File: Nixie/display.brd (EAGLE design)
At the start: 111.4 x 49.5 mm, 21 parts, among them IC1 74LS595N, IC2 74LS595N

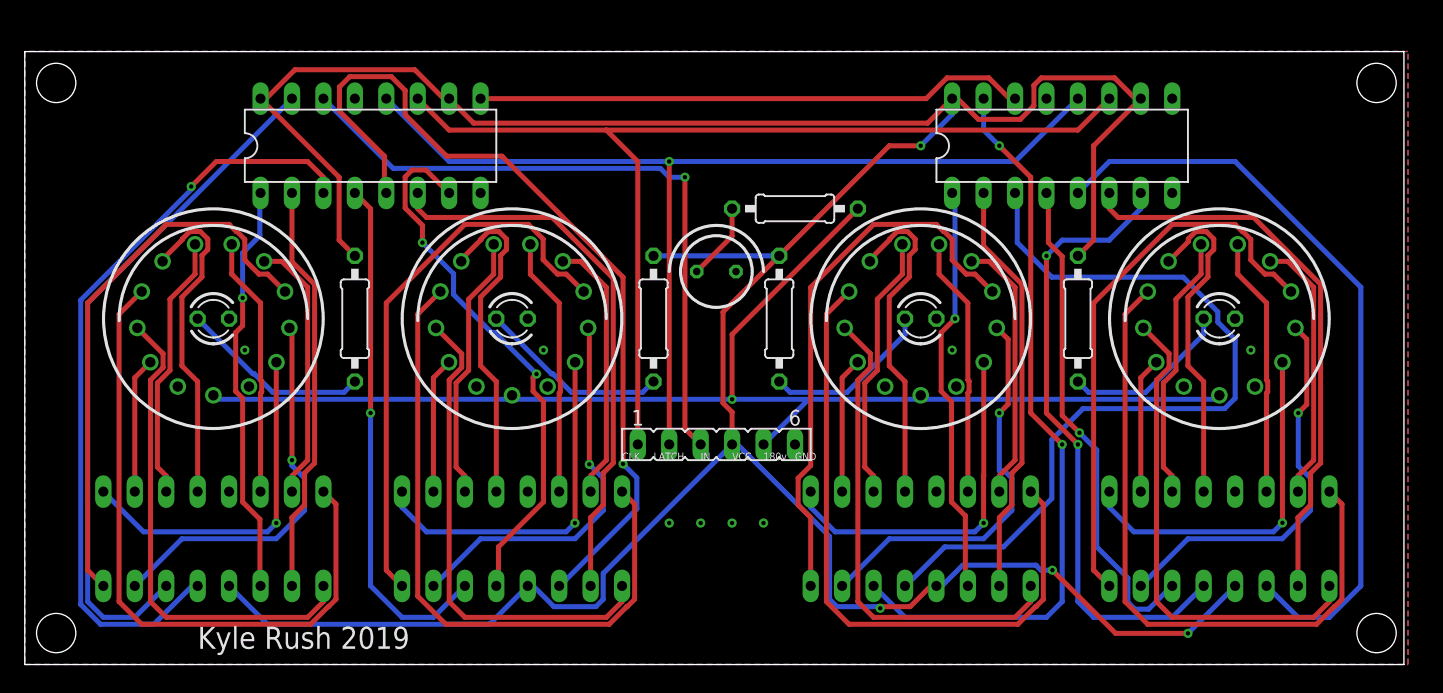
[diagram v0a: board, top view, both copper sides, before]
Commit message: Stable PSU, TPIC6b595 working. Release candidate
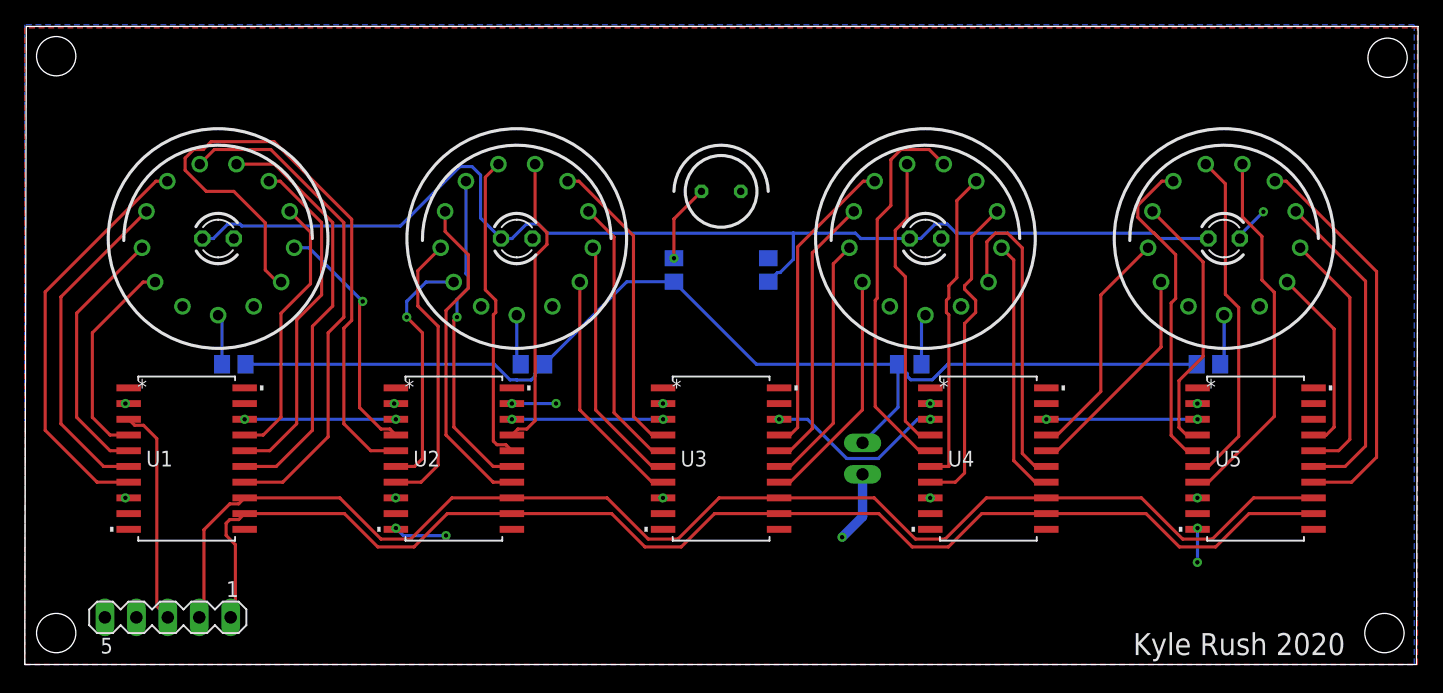
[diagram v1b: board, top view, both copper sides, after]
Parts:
- removed IC1, IC2: 74LS595N, 74xx-us:DIL16
- removed U$1, U$2, U$3, U$4: NTE74141, NTE74141:DIP-16(DIL-16)
- added R6: (no value), rcl:R0805
- added U1, U2, U3, U4, U5: TPIC6B595DWRG4, Digikey:DW20
- added X1: 22-23-2021, con-molex:22-23-2021
- R1: value 330 Ohm -> 330; device rcl:0207/10 -> rcl:R0805
- R2: value 330 Ohm -> 68k; device rcl:0207/10 -> rcl:R0805
- R3, R4: value 330 Ohm -> (none); device rcl:0207/10 -> rcl:R0805
- R5: value 68 kOhm -> (none); device rcl:0207/10 -> rcl:R0805
- SV1: device con-lsta:FE06 -> con-lstb:MA05-1
- moved SV1 46.5 mm to (11.6, 3.81), turned to 180 degrees
- moved R3 44.2 mm to (16.9, 24.3), flipped to the bottom, turned to 180 degrees
- moved R4 44.2 mm to (41.0, 24.3), flipped to the bottom, turned to 180 degrees
- moved R1 33.6 mm to (60.1, 31.9), flipped to the bottom, turned to 90 degrees
- moved R5 15.6 mm to (71.5, 24.3), flipped to the bottom, turned to 0 degrees
- moved LED1 6.49 mm to (15.6, 34.4)
- moved LED2 6.49 mm to (39.8, 34.4)
- moved LED3 6.49 mm to (72.8, 34.4)
- moved LED4 6.49 mm to (96.9, 34.4)
- moved N1 6.49 mm to (15.6, 34.4)
- moved N2 6.49 mm to (39.8, 34.4)
- moved N3 6.49 mm to (72.8, 34.4)
- moved N4 6.49 mm to (96.9, 34.4)
- moved N5 6.49 mm to (56.3, 38.2)
- moved R2 4.27 mm to (52.5, 31.9), flipped to the bottom, turned to 90 degrees
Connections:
- removed net CLOCK: IC1.11, IC2.11, SV1.1
- removed net IN: IC1.14, SV1.3
- removed net LATCH: IC1.12, IC2.12, SV1.2
- removed net N$50: IC2.1, U$3.6
- removed net N$51: IC2.2, U$3.7
- removed net N$53: IC2.4, U$4.3
- removed net N$54: IC2.5, U$4.6
- removed net N$55: IC2.6, U$4.7
- removed net N$56: IC2.7, U$4.4
- removed net N$57: IC1.9, IC2.14
- removed net N$58: LED1.A, R1.2
- removed net N$59: LED2.A, R2.2
- removed net N$60: LED3.A, R3.2
- removed net N$61: LED4.A, R4.2
- removed net N$62: N5.A, R5.2
- new net N$77: U1.18, U2.3
- new net N$78: U2.18, U3.3
- new net N$79: U3.18, U4.3
- net GND: now also SV1.5, U1.10, U1.11, U1.19, U1.9, U2.10, U2.11, U2.19, U2.9, U3.10, U3.11, U3.19, U3.9, U4.10, U4.11, U4.19, U4.9, U5.10, U5.11, U5.19, U5.9, X1.2; no longer IC1.13, IC1.8, IC2.13, IC2.8, SV1.6, U$1.12, U$2.12, U$3.12, U$4.12
- net N$1: now also N1.1, U1.4; no longer N1.0, U$1.16
- net N$10: now also N1.0, U2.5; no longer N1.9, U$1.2
- net N$11: now also N2.1, U2.6; no longer N2.0, U$2.16
- net N$12: now also N2.2, U2.7; no longer N2.1, U$2.15
- net N$13: now also N2.3, U2.14; no longer N2.2, U$2.8
- net N$14: now also N2.4, U2.15; no longer N2.3, U$2.9
- net N$15: now also N2.5, U2.16; no longer N2.4, U$2.13
- net N$16: now also N2.6, U2.17; no longer N2.5, U$2.14
- net N$17: now also N2.7, U3.4; no longer N2.6, U$2.11
- net N$18: now also N2.8, U3.5; no longer N2.7, U$2.10
- net N$19: now also N2.9, U3.6; no longer N2.8, U$2.1
- net N$2: now also N1.2, U1.5; no longer N1.1, U$1.15
- net N$20: now also N2.0, U3.7; no longer N2.9, U$2.2
- net N$21: now also LED1.A, LED2.A, LED3.A, LED4.A, R1.1; no longer IC1.15, U$1.3
- net N$22: now also N5.A, R2.2; no longer IC1.1, U$1.6
- net N$23: now also N1.A, R3.1; no longer IC1.2, U$1.7
- net N$24: now also N2.A, R4.1; no longer IC1.3, U$1.4
- net N$25: now also N3.A, R5.1; no longer IC1.4, U$2.3
- net N$26: now also N4.A, R6.1; no longer IC1.5, U$2.6
- net N$27: now also U4.18, U5.3; no longer IC1.6, U$2.7
- net N$28: now also SV1.1, U1.12, U2.12, U3.12, U4.12, U5.12; no longer IC1.7, U$2.4
- net N$29: now also N3.1, U3.14; no longer N3.0, U$3.16
- net N$3: now also N1.3, U1.6; no longer N1.2, U$1.8
- net N$30: now also N3.2, U3.15; no longer N3.1, U$3.15
- net N$31: now also N3.3, U3.16; no longer N3.2, U$3.8
- net N$32: now also N3.4, U3.17; no longer N3.3, U$3.9
- net N$33: now also N3.8, U4.7; no longer N3.4, U$3.13
- net N$34: now also N3.6, U4.5; no longer N3.5, U$3.14
- net N$35: now also N3.9, U4.14; no longer N3.6, U$3.11
- net N$36: now also N3.5, U4.4; no longer N3.7, U$3.10
- net N$37: now also N3.7, U4.6; no longer N3.8, U$3.1
- net N$38: now also N3.0, U4.15; no longer N3.9, U$3.2
- net N$39: now also N4.1, U4.16; no longer N4.0, U$4.16
- net N$4: now also N1.4, U1.7; no longer N1.3, U$1.9
- net N$40: now also N4.2, U4.17; no longer N4.1, U$4.15
- net N$41: now also N4.0, U5.17; no longer N4.2, U$4.8
- net N$42: now also N4.9, U5.16; no longer N4.3, U$4.9
- net N$43: now also N4.8, U5.15; no longer N4.4, U$4.13
- net N$44: now also N4.7, U5.14; no longer N4.5, U$4.14
- net N$45: now also U5.7; no longer U$4.11
- net N$46: now also N4.5, U5.6; no longer N4.7, U$4.10
- net N$47: now also N4.4, U5.5; no longer N4.8, U$4.1
- net N$48: now also N4.3, U5.4; no longer N4.9, U$4.2
- net N$49: now also SV1.2, U1.13, U2.13, U3.13, U4.13, U5.13; no longer IC2.15, U$3.3
- net N$5: now also N1.5, U1.14; no longer N1.4, U$1.13
- net N$52: now also SV1.3, U1.3; no longer IC2.3, U$3.4
- net N$6: now also N1.6, U1.15; no longer N1.5, U$1.14
- net N$7: now also N1.7, U1.16; no longer N1.6, U$1.11
- net N$8: now also N1.8, U1.17; no longer N1.7, U$1.10
- net N$9: now also N1.9, U2.4; no longer N1.8, U$1.1
- net V+: now also R2.1, R3.2, R4.2, R5.2, R6.2, X1.1; no longer N1.A, N2.A, N3.A, N4.A, R5.1, SV1.5
- net VCC: now also R1.2, U1.2, U1.8, U2.2, U2.8, U3.2, U3.8, U4.2, U4.8, U5.2, U5.8; no longer IC1.10, IC1.16, IC2.10, IC2.16, R1.1, R2.1, R3.1, R4.1, U$1.5, U$2.5, U$3.5, U$4.5
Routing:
- net VCC: track 261.6 -> 0.00 mm, vias 4 -> 10
- net CLOCK: track 84.4 -> 0.00 mm
- net LATCH: track 82.9 -> 0.00 mm, vias 1 -> 0
- net N$26: track 69.3 -> 4.10 mm, vias 1 -> 0
- net N$54: track 62.0 -> 0.00 mm
- net N$28: track 44.2 -> 105.2 mm, vias 2 -> 0
- net N$24: track 62.3 -> 4.10 mm, vias 1 -> 0
- net IN: track 54.0 -> 0.00 mm, vias 1 -> 0
- net N$56: track 51.2 -> 0.00 mm, vias 2 -> 0
- net N$49: track 60.1 -> 109.0 mm, vias 2 -> 0
- net N$52: track 65.9 -> 17.7 mm
- net N$55: track 46.0 -> 0.00 mm
- net N$57: track 44.6 -> 0.00 mm
- net N$53: track 40.4 -> 0.00 mm, vias 1 -> 0
- net N$21: track 55.4 -> 95.1 mm
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- added copper zone on layer 16, net VCC
- removed copper zone on layer 16, net GND
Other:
- board size 111.4 x 49.5 mm -> 112.6 x 51.6 mm
- board text added: "Kyle Rush 2020"
- board text removed: "180v"
- board text removed: "CLK"
- board text removed: "GND"
- board text removed: "IN"
- board text removed: "Kyle Rush 2019"
- board text removed: "LATCH"
- board text removed: "VCC"

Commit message: Production ready board with BOMS
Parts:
- R3, R4, R5, R6: value (none) -> 15k
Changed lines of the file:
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@@
 <attribute name="VALUE" x="98.806" y="32.766" size="1.27" layer="27" ratio="10"/>
 </element>
-<element name="R3" library="rcl" library_urn="urn:adsk.eagle:library:334" package="R0805" package3d_urn="urn:adsk.eagle:package:23553/2" value="" x="16.891" y="24.257" smashed="yes" rot="MR180">
+<element name="R3" library="rcl" library_urn="urn:adsk.eagle:library:334" package="R0805" package3d_urn="urn:adsk.eagle:package:23553/2" value="15k" x="16.891" y="24.257" smashed="yes" rot="MR180">
 <attribute name="NAME" x="16.256" y="22.987" size="1.27" layer="26" rot="MR180"/>
 <attribute name="POPULARITY" value="85" x="16.891" y="24.257" size="1.778" layer="28" rot="MR180" display="off"/>
@@
 <attribute name="VENDOR" value="Texas Instruments" x="34.671" y="16.637" size="1.778" layer="27" display="off"/>
 </element>
-<element name="R4" library="rcl" library_urn="urn:adsk.eagle:library:334" package="R0805" package3d_urn="urn:adsk.eagle:package:23553/2" value="" x="41.021" y="24.257" smashed="yes" rot="MR180">
+<element name="R4" library="rcl" library_urn="urn:adsk.eagle:library:334" package="R0805" package3d_urn="urn:adsk.eagle:package:23553/2" value="15k" x="41.021" y="24.257" smashed="yes" rot="MR180">
 <attribute name="NAME" x="40.386" y="22.987" size="1.27" layer="26" rot="MR180"/>
 <attribute name="POPULARITY" value="85" x="41.021" y="24.257" size="1.778" layer="28" rot="MR180" display="off"/>
@@
 <attribute name="VALUE" x="40.386" y="26.797" size="1.27" layer="28" rot="MR180"/>
 </element>
-<element name="R5" library="rcl" library_urn="urn:adsk.eagle:library:334" package="R0805" package3d_urn="urn:adsk.eagle:package:23553/2" value="" x="71.501" y="24.257" smashed="yes" rot="MR0">
+<element name="R5" library="rcl" library_urn="urn:adsk.eagle:library:334" package="R0805" package3d_urn="urn:adsk.eagle:package:23553/2" value="15k" x="71.501" y="24.257" smashed="yes" rot="MR0">
 <attribute name="NAME" x="72.136" y="25.527" size="1.27" layer="26" rot="MR0"/>
 <attribute name="POPULARITY" value="85" x="71.501" y="24.257" size="1.778" layer="28" rot="MR0" display="off"/>
@@
 <attribute name="VALUE" x="72.136" y="21.717" size="1.27" layer="28" rot="MR0"/>
 </element>
-<element name="R6" library="rcl" library_urn="urn:adsk.eagle:library:334" package="R0805" package3d_urn="urn:adsk.eagle:package:23553/2" value="" x="95.631" y="24.257" smashed="yes" rot="MR0">
+<element name="R6" library="rcl" library_urn="urn:adsk.eagle:library:334" package="R0805" package3d_urn="urn:adsk.eagle:package:23553/2" value="15k" x="95.631" y="24.257" smashed="yes" rot="MR0">
 <attribute name="NAME" x="96.266" y="25.527" size="1.27" layer="26" rot="MR0"/>
 <attribute name="POPULARITY" value="85" x="95.631" y="24.257" size="1.778" layer="28" rot="MR0" display="off"/>
